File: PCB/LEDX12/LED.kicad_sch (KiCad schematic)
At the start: 33 parts, among them J1 Conn_01x03, J2 TC2030-USB-NL-DS, P1 Square, P2 Square, P3 Square, P4 Square, U1 TPS562246, U2 ESP32-S3-MINI-1, U3 ICS43434_MEMS_Mic

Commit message: Library update
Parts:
- J1: footprint RevK:WAGO-2060-453-998-404-S -> RevK:WAGO-2060-453-998-404-O
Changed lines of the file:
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@@
 			)
 		)
-		(property "Footprint" "RevK:WAGO-2060-453-998-404-S"
+		(property "Footprint" "RevK:WAGO-2060-453-998-404-O"
 			(at 201.295 97.155 0)
 			(effects

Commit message: Updated (thicker case)
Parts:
- R4: MPN (none) -> C473048
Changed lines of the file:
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@@
+			)
+		)
+		(property "MPN" "C473048"
+			(at 135.255 102.87 90)
+			(effects
+				(font
+					(size 1.27 1.27)
+				)
+				(hide yes)
 			)
 		)

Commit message: Spacing
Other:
- note added: "Clean up GPIOs"
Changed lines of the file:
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@@
 		(comment 2 "www.me.uk")
+	)
+	(text "Clean up GPIOs"
+		(exclude_from_sim no)
+		(at 129.54 140.462 0)
+		(effects
+			(font
+				(size 12.7 12.7)
+			)
+		)
 	)
 	(junction

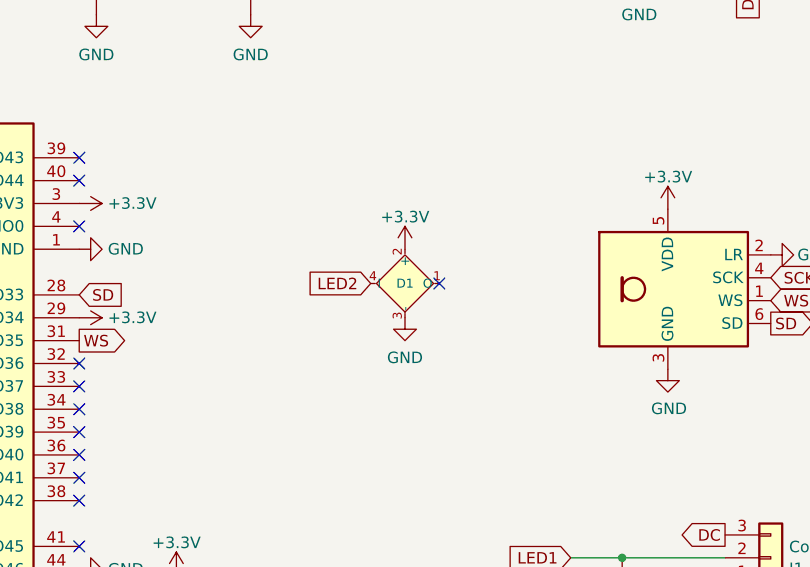
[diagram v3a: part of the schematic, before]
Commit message: New LEDs
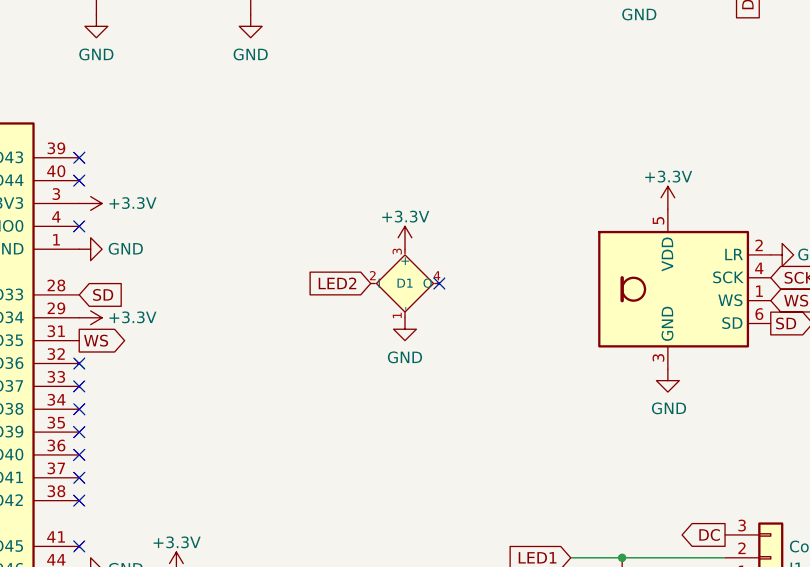
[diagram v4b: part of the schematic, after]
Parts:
- D1: footprint RevK:SMD1010 -> RevK:SMD1615; symbol RevK:WS2812B-1mm -> RevK:WS2812B-1.5mm; MPN C5349953 -> C5349954
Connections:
- net +3.3V: now also D1.3 (+); no longer D1.2 (+)
- net GND: now also D1.1 (-); no longer D1.3 (-)
- net LED2: now also D1.2 (I); no longer D1.4 (I)
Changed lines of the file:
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@@
 	)
 	(symbol
-		(lib_id "RevK:WS2812B-1mm")
+		(lib_id "RevK:WS2812B-1.5mm")
 		(at 160.655 66.675 0)
-		(mirror x)
 		(unit 1)
 		(exclude_from_sim no)
@@
 		)
 		(property "Value" "XL-1010RGBC-WS2812B"
-			(at 161.925 60.96 0)
+			(at 161.925 72.39 0)
 			(effects
 				(font
@@
 			)
 		)
-		(property "Footprint" "RevK:SMD1010"
+		(property "Footprint" "RevK:SMD1615"
 			(at 161.925 59.055 0)
 			(effects
@@
 			)
 		)
-		(property "Datasheet" "https://datasheet.lcsc.com/lcsc/2301111010_XINGLIGHT-XL-1010RGBC-WS2812B_C5349953.pdf"
+		(property "Datasheet" "https://www.lcsc.com/datasheet/C5349954.pdf"
 			(at 161.925 57.15 0)
 			(effects
@@
 			)
 		)
-		(property "MPN" "C5349953"
+		(property "MPN" "C5349954"
 			(at 161.925 55.245 0)
 			(effects

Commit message: Library update
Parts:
- added D6: MBR0530, RevK:D_SOD-123, symbol Diode:1N5819
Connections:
- net DC: now also D6.1 (K); no longer C1.1, C12.1, C16.1, C2.1, J1.3 (Pin_3)
- new net: C1.1, C12.1, C16.1, C2.1, D6.2 (A), J1.3 (Pin_3)
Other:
- note removed: "Clean up GPIOs"
- moved on the sheet: C1, C10, C11, C12, C13, C15, C16, C2, C3, C8, D2, J1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
